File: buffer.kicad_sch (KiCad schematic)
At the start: 17 parts, among them J8 AudioPlug3, U3 OPA1622

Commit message: Small tunes and adjustments before Inventree work.
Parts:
- removed J8: AudioPlug3, Connector_Audio:Jack_3.5mm_CUI_SJ-3523-SMT_Horizontal, symbol Connector_Audio:AudioPlug3
- added J8: AudioJack3, symbol Connector_Audio:AudioJack3
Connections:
- net GND: now also J8.S
- net HEADPHONES_LEFT: now also J8.T
- net HEADPHONES_RIGHT: now also J8.R
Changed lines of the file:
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@@
 	(title_block
 		(title "${PROJECT_NAME}")
-		(date "2026-08-25")
+		(date "2026-08-29")
 		(rev "${REVISION}")
 		(comment 1 "${PCBA_IPN}")
@@
 				(path "/62ffec33-ae93-49a8-bfe6-566578dd8e82/8fba3b35-d615-47af-8081-02211a3ffbd2"
 					(reference "#PWR043")
-					(unit 1)
-				)
-			)
-		)
-	)
-	(symbol
-		(lib_id "Connector_Audio:AudioPlug3")
-		(at 236.22 105.41 180)
-		(unit 1)
-		(body_style 1)
-		(exclude_from_sim no)
-		(in_bom yes)
-		(on_board yes)
-		(in_pos_files yes)
-		(dnp no)
-		(fields_autoplaced yes)
-		(property "Reference" "J8"
-			(at 250.19 104.1399 0)
-			(show_name no)
-			(do_not_autoplace no)
-			(effects
-				(font
-					(size 1.27 1.27)
-				)
-				(justify right)
-			)
-		)
-		(property "Value" "AudioPlug3"
-			(at 250.19 106.6799 0)
-			(show_name no)
-			(do_not_autoplace no)
-			(effects
-				(font
-					(size 1.27 1.27)
-				)
-				(justify right)
-			)
-		)
-		(property "Footprint" "Connector_Audio:Jack_3.5mm_CUI_SJ-3523-SMT_Horizontal"
-			(at 233.68 104.14 0)
-			(hide yes)
-			(show_name no)
-			(do_not_autoplace no)
-			(effects
-				(font
-					(size 1.27 1.27)
-				)
-			)
-		)
-		(property "Datasheet" ""
-			(at 233.68 104.14 0)
-			(hide yes)
-			(show_name no)
-			(do_not_autoplace no)
-			(effects
-				(font
-					(size 1.27 1.27)
-				)
-			)
-		)
-		(property "Description" "Audio Jack, 3 Poles (Stereo / TRS)"
-			(at 236.22 105.41 0)
-			(hide yes)
-			(show_name no)
-			(do_not_autoplace no)
-			(effects
-				(font
-					(size 1.27 1.27)
-				)
-			)
-		)
-		(pin "R"
-		)
-		(pin "S"
-		)
-		(pin "T"
-		)
-		(instances
-			(project "headphone_amp"
-				(path "/62ffec33-ae93-49a8-bfe6-566578dd8e82/8fba3b35-d615-47af-8081-02211a3ffbd2"
-					(reference "J8")
 					(unit 1)
 				)
@@
 					(unit 1)
 				)
+			)
+		)
+	)
+	(symbol
+		(lib_id "Connector_Audio:AudioJack3")
+		(at 226.06 105.41 180)
+		(unit 1)
+		(body_style 1)
+		(exclude_from_sim no)
+		(in_bom yes)
+		(on_board yes)
+		(in_pos_files yes)
+		(dnp no)
+		(property "Reference" "J8"
+			(at 227.965 114.3 0)
+			(show_name no)
+			(do_not_autoplace no)
+			(effects
+				(font
+					(size 1.27 1.27)
+				)
+			)
+		)
+		(property "Value" "AudioJack3"
+			(at 227.965 111.76 0)
+			(show_name no)
+			(do_not_autoplace no)
+			(effects
+				(font
+					(size 1.27 1.27)
+				)
+			)
+		)
+		(property "Footprint" ""
+			(at 226.06 105.41 0)
+			(hide yes)
+			(show_name no)
+			(do_not_autoplace no)
+			(effects
+				(font
+					(size 1.27 1.27)
+				)
+			)
+		)
+		(property "Datasheet" ""
+			(at 226.06 105.41 0)
+			(hide yes)
+			(show_name no)
+			(do_not_autoplace no)
+			(effects
+				(font
+					(size 1.27 1.27)
+				)
+			)
+		)
+		(property "Description" "Audio Jack, 3 Poles (Stereo / TRS)"
+			(at 226.06 105.41 0)
+			(hide yes)
+			(show_name no)
+			(do_not_autoplace no)
+			(effects
+				(font
+					(size 1.27 1.27)
+				)
+			)
+		)
+		(pin "T"
+		)
+		(pin "R"
+		)
+		(pin "S"
+		)
+		(instances
+			(project "headphone_amp"
+				(path "/62ffec33-ae93-49a8-bfe6-566578dd8e82/8fba3b35-d615-47af-8081-02211a3ffbd2"
+					(reference "J8")
+					(unit 1)
+				)

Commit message: Started Inventree work.
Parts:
- C18, C19: value 875105244013 -> 220uF; footprint (none) -> cap_polymer:WCAP-PSLP_6.3X5.8_DXL_; symbol Device:C_Polarized_US -> #inventree_kicad:C_220U_ALU_POLY_10V_SMD; IPN (none) -> 301-0006; InvenTree (none) -> 29; Part URL (none) -> http://10.0.0.33/web/part/29/
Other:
- moved on the sheet: C17, C18, C19, C32, C34, C35, J8, R25, R26, R27, R28, R48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

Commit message: Corrected issues Claude identified, added 'poor man's cab filter' on recovery stage per Ihsan.
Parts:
- added D7: CD0603-B0340R, Diode_SMD:D_0603_1608Metric, symbol Device:D_Schottky_Filled
- added R40, R54: 100K, Resistor_SMD:R_0402_1005Metric, symbol inventree_kicad:R_100K_0402_1PCT_0W0625
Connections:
- net 9V: now also D7.1 (K)
- net EN: now also D7.2 (A)
- net GND: now also R40.2, R54.2
- net HEADPHONES_LEFT: now also R40.1
- net HEADPHONES_RIGHT: now also R54.1

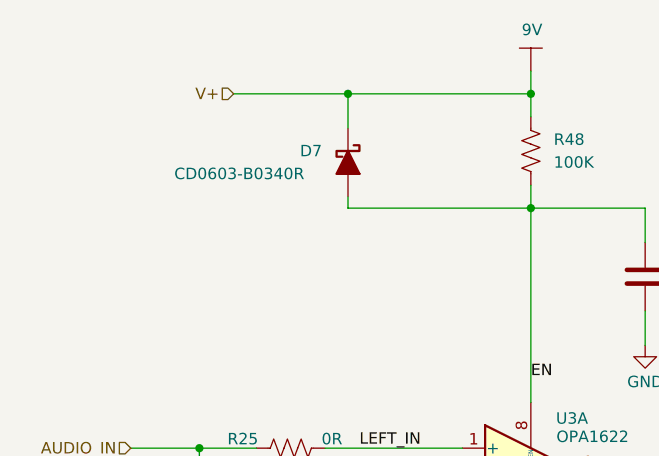
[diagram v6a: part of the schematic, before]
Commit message: Added schottky symbol in inventree and category to kicad categories.
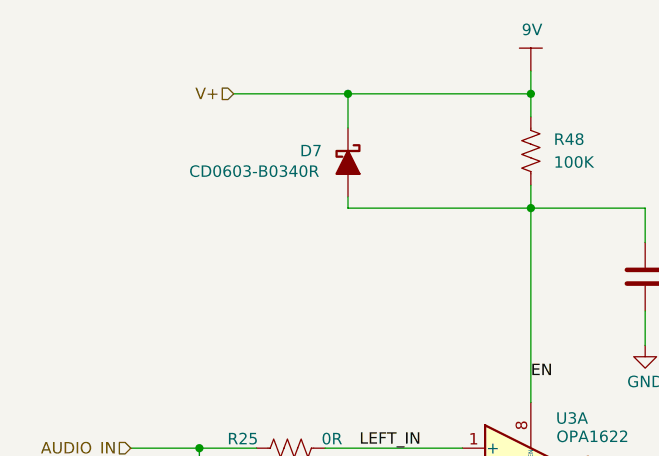
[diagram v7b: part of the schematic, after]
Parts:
- D7: symbol Device:D_Schottky_Filled -> inventree_kicad:D_SCHOTTKY_40V_300MA_0603; IPN (none) -> 306-0002; InvenTree (none) -> 31; Part URL (none) -> http://10.0.0.33/web/part/31/
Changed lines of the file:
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@@
 	)
 	(symbol
-		(lib_id "Device:D_Schottky_Filled")
+		(lib_id "inventree_kicad:D_SCHOTTKY_40V_300MA_0603")
 		(at 77.47 43.18 270)
 		(unit 1)
@@
 		)
 		(property "Value" "CD0603-B0340R"
-			(at 58.166 44.45 90)
+			(at 67.056 44.196 90)
 			(show_name no)
 			(do_not_autoplace no)
@@
 					(size 1.27 1.27)
 				)
-				(justify left)
 			)
 		)
@@
 			)
 		)
-		(property "Datasheet" ""
+		(property "Datasheet" "https://www.bourns.com/docs/product-datasheets/cd0603-b.pdf"
 			(at 77.47 43.18 0)
 			(hide yes)
@@
 			)
 		)
-		(property "Description" "Schottky diode, filled shape"
+		(property "Description" "Diode 40 V 300mA Surface Mount 0603 (1608 Metric)"
 			(at 77.47 43.18 0)
 			(hide yes)
+			(show_name no)
+			(do_not_autoplace no)
+			(effects
+				(font
+					(size 1.27 1.27)
+				)
+			)
+		)
+		(property "InvenTree" "31"
+			(at 77.47 43.18 0)
+			(hide yes)
+			(show_name no)
+			(do_not_autoplace no)
+			(effects
+				(font
+					(size 1.27 1.27)
+				)
+			)
+		)
+		(property "Part URL" "http://10.0.0.33/web/part/31/"
+			(at 77.47 43.18 0)
+			(hide yes)
+			(show_name no)
+			(do_not_autoplace no)
+			(effects
+				(font
+					(size 1.27 1.27)
+				)
+			)
+		)
+		(property "IPN" "306-0002"
+			(at 77.47 43.18 0)
+			(hide yes)

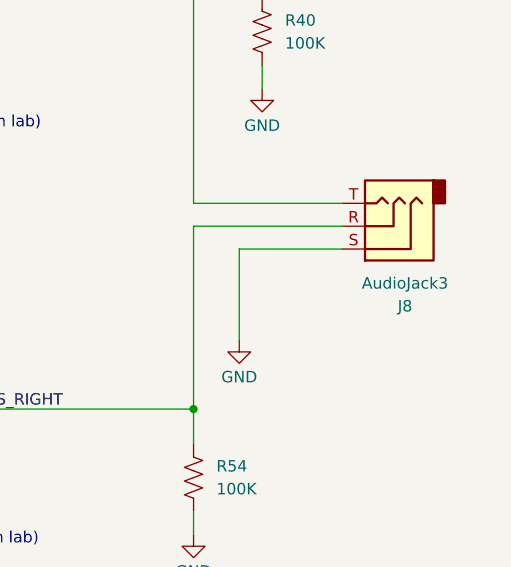
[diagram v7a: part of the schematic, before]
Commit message: Updated theory doc, started layout, fixed a footprint.
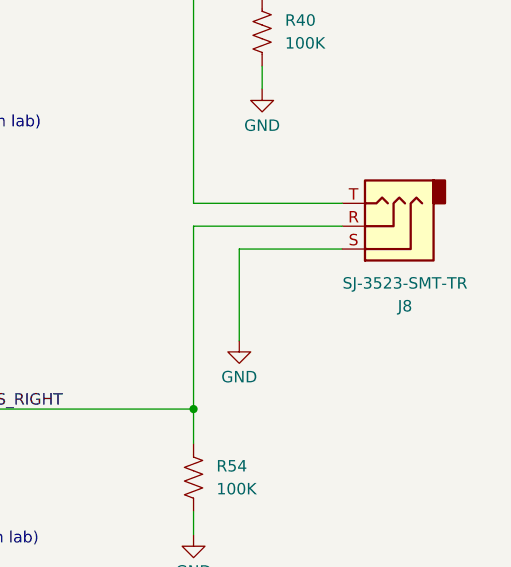
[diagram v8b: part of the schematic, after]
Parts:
- J8: value AudioJack3 -> SJ-3523-SMT-TR; footprint (none) -> Connector_Audio:Jack_3.5mm_CUI_SJ-3523-SMT_Horizontal
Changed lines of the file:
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@@
 			)
 		)
-		(property "Value" "AudioJack3"
+		(property "Value" "SJ-3523-SMT-TR"
 			(at 249.555 110.49 0)
 			(show_name no)
@@
 			)
 		)
-		(property "Footprint" ""
+		(property "Footprint" "Connector_Audio:Jack_3.5mm_CUI_SJ-3523-SMT_Horizontal"
 			(at 247.65 104.14 0)
 			(hide yes)
